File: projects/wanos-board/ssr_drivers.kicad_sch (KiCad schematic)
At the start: 21 parts, among them J13 SSR_FIELD, Q1 PN2222A, Q2 PN2222A, Q3 PN2222A, Q4 PN2222A, Q5 PN2222A

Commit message: pi_power & 12V_monitor schematics OK added datasheets doc update
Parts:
- Q1, Q2, Q3, Q4: value PN2222A -> PN2222A-TA; footprint Package_TO_SOT_THT:TO-92_Inline -> Package_TO_SOT_SMD:SOT-23
- Q5: value PN2222A -> PN2222A-TA; footprint (none) -> Package_TO_SOT_SMD:SOT-23

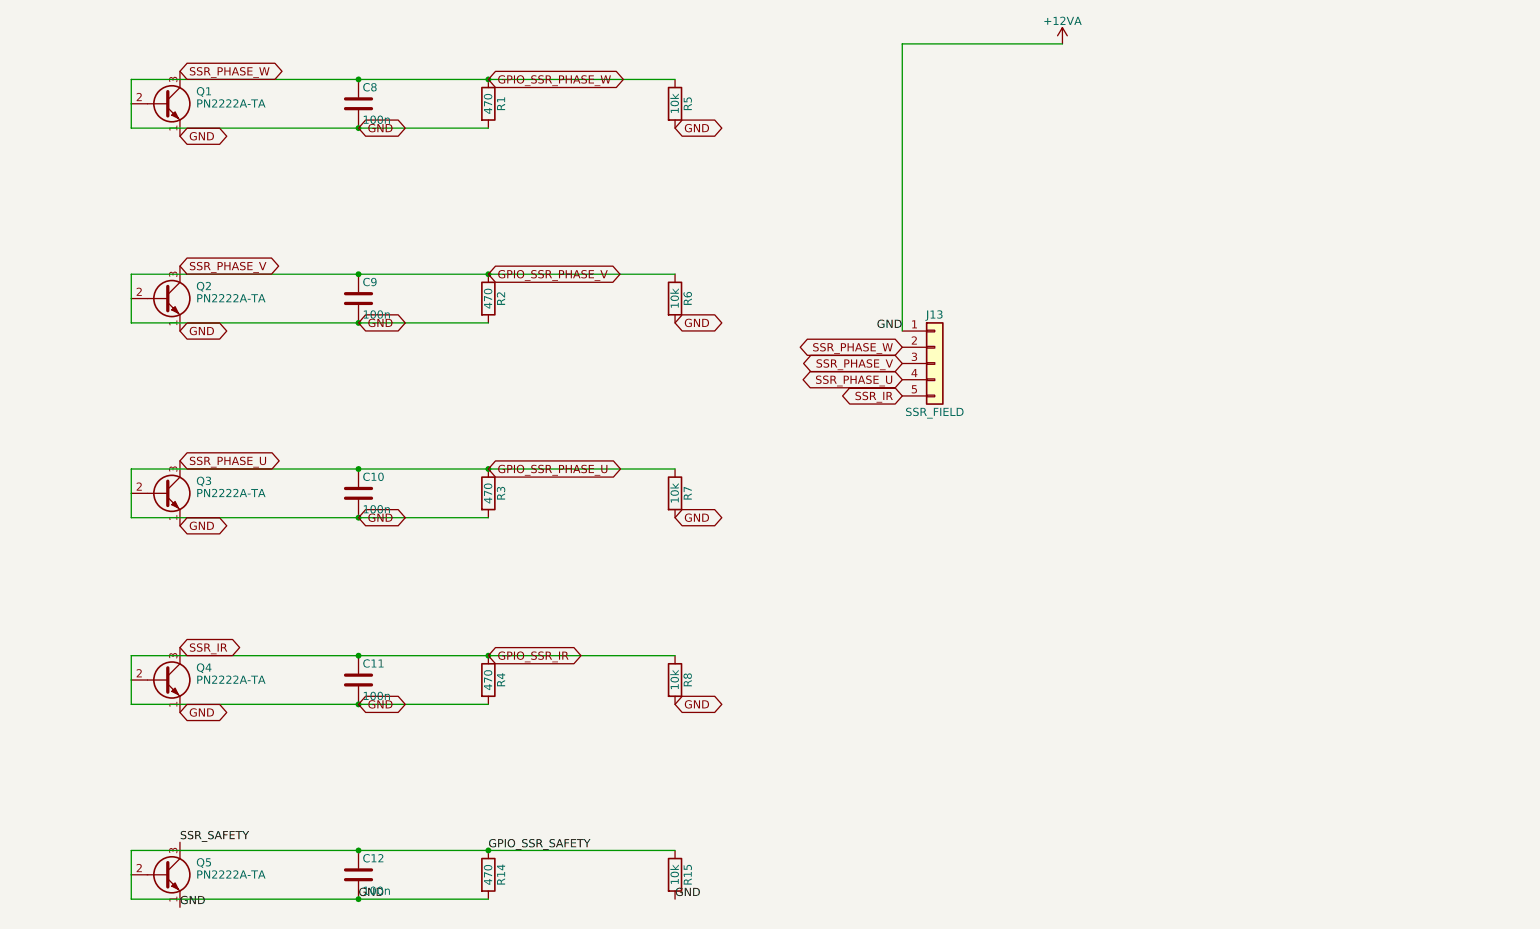
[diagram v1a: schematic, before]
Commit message: SSR, power, IO_expander schemas update
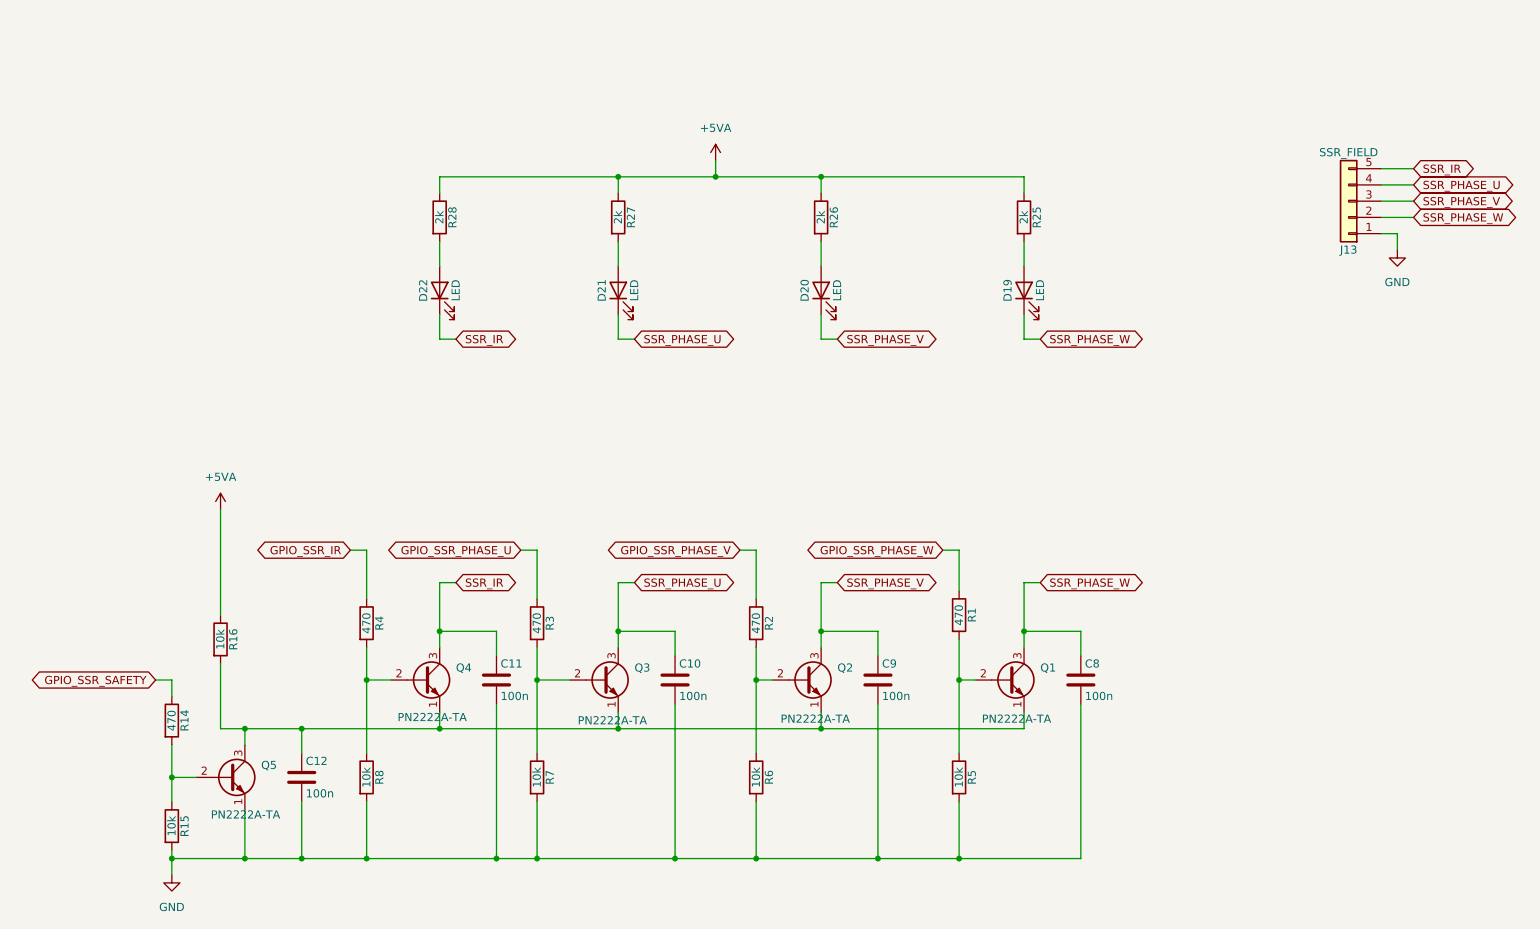
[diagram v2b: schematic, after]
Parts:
- added D19, D20, D21, D22: LED, LED_SMD:LED_0805_2012Metric, symbol Device:LED
- added R16: 10k, symbol Device:R
- added R25, R26, R27, R28: 2k, Resistor_SMD:R_0805_2012Metric, symbol Device:R
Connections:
- net SSR_IR: now also C11.1, D22.1 (K)
- net SSR_PHASE_U: now also C10.1, D21.1 (K)
- net SSR_PHASE_V: now also C9.1, D20.1 (K)
- net SSR_PHASE_W: now also C8.1, D19.1 (K)
- removed net +12VA: C10.1, C10.2, C11.1, C11.2, C12.1, C12.2, C8.1, C8.2, C9.1, C9.2, J13.1 (Pin_1), Q1.1 (E), Q1.2 (B), Q2.1 (E), Q2.2 (B), Q3.1 (E), Q3.2 (B), Q4.1 (E), Q4.2 (B), Q5.1 (E), Q5.2 (B), R1.1, R1.2, R14.1, R14.2, R15.1, R15.2, R2.1, R2.2, R3.1, R3.2, R4.1, R4.2, R5.1, R5.2, R6.1, R6.2, R7.1, R7.2, R8.1, R8.2
- net SSR_SAFETY: no longer names the net of Q5.3 (C)
- net SSR_SAFETY: now also C12.1, Q1.1 (E), Q2.1 (E), Q3.1 (E), Q4.1 (E), R16.2
- new net: Q5.2 (B), R14.2, R15.1
- new net: D21.2 (A), R27.2
- new net: Q1.2 (B), R1.2, R5.1
- new net: Q4.2 (B), R4.2, R8.1
- new net: Q2.2 (B), R2.2, R6.1
- new net: D22.2 (A), R28.2
- new net: D20.2 (A), R26.2
- new net: D19.2 (A), R25.2
- new net: Q3.2 (B), R3.2, R7.1
- new net +5VA: R16.1, R25.1, R26.1, R27.1, R28.1
- new net GND: C10.2, C11.2, C12.2, C8.2, C9.2, J13.1 (Pin_1), Q5.1 (E), R15.2, R5.2, R6.2, R7.2, R8.2
- new net GPIO_SSR_IR: R4.1
- new net GPIO_SSR_PHASE_U: R3.1
- new net GPIO_SSR_PHASE_V: R2.1
- new net GPIO_SSR_PHASE_W: R1.1
- new net GPIO_SSR_SAFETY: R14.1
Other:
- moved on the sheet: C10, C11, C12, C8, C9, J13, Q1, Q2, Q3, Q4, Q5, R1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
